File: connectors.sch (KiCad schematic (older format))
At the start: 4 parts

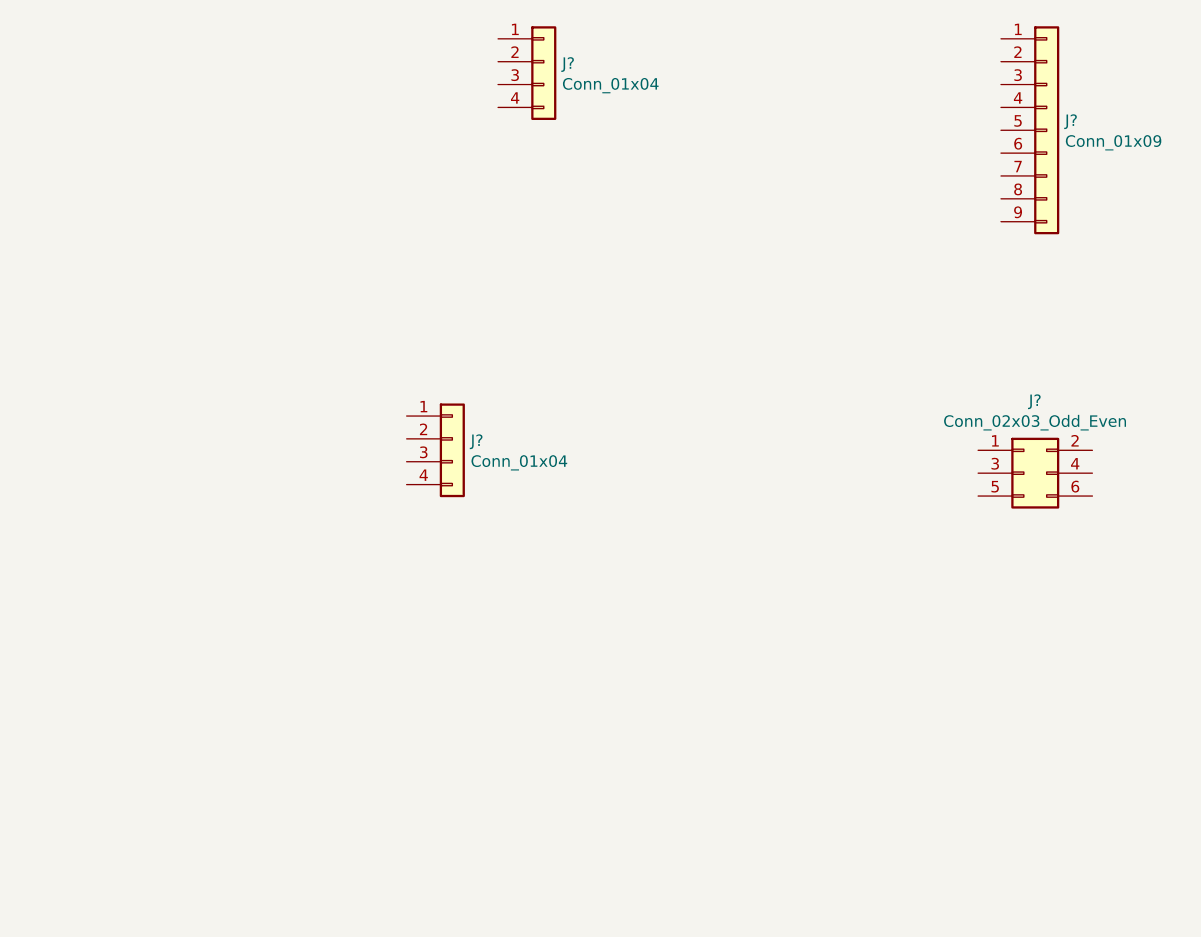
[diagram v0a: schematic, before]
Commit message: Add a new symbol library DS1337_AH to Ahmad library
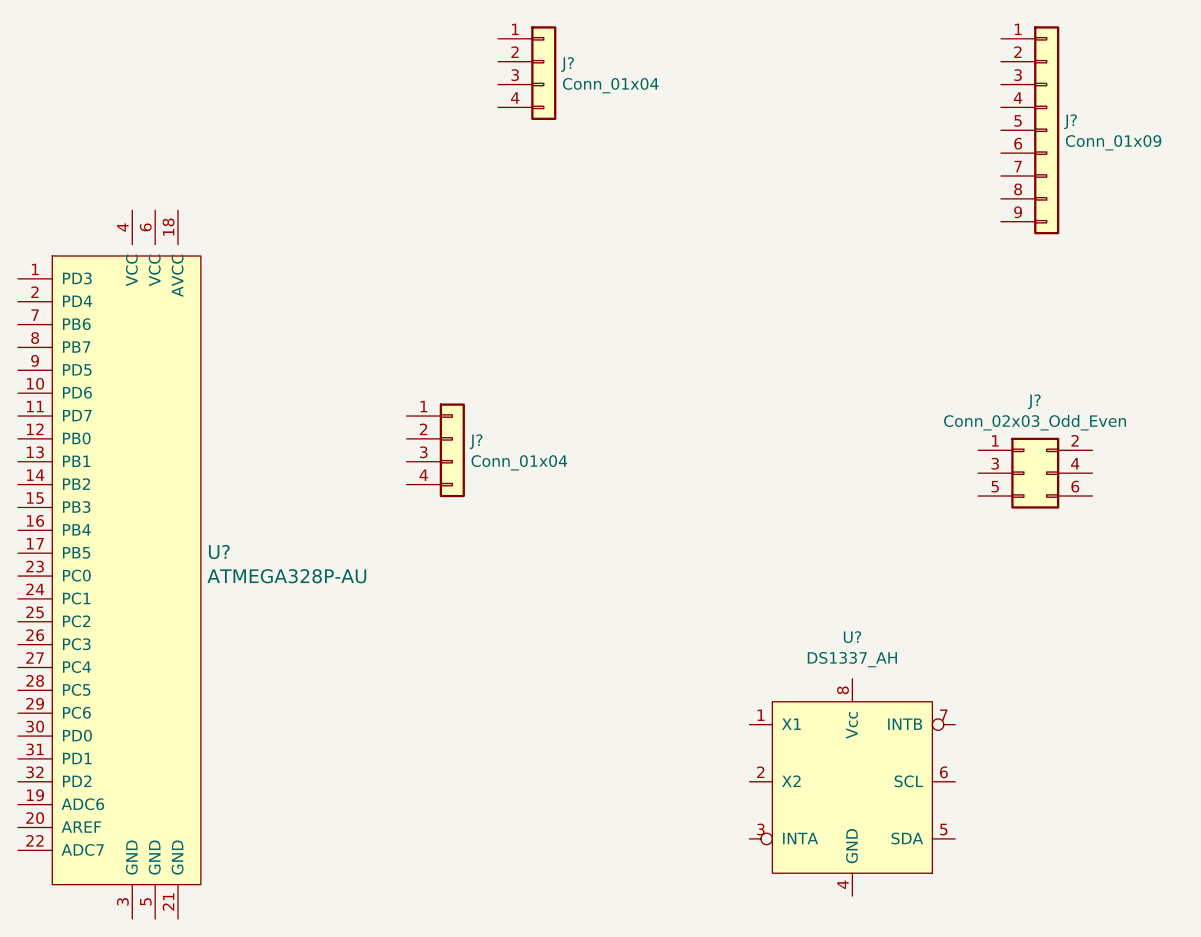
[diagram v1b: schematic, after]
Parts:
- added U?: ATMEGA328P-AU, digikey-footprints:TQFP-32_7x7mm, symbol dk_Embedded-Microcontrollers:ATMEGA328P-AU
- added U?: DS1337_AH, symbol Ahmad_Library:DS1337_AH
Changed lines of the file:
@@
+	1    0    0    -1
+$EndComp
+$Comp
+L dk_Embedded-Microcontrollers:ATMEGA328P-AU U?
+U 1 1 615F99BF
+P 3450 4050
+F 0 "U?" H 3778 4153 60  0000 L CNN
+F 1 "ATMEGA328P-AU" H 3778 4047 60  0000 L CNN
+F 2 "digikey-footprints:TQFP-32_7x7mm" H 3650 4250 60  0001 L CNN
+F 3 "http://www.microchip.com/mymicrochip/filehandler.aspx?ddocname=en608326" H 3650 4350 60  0001 L CNN
+F 4 "ATMEGA328P-AU-ND" H 3650 4450 60  0001 L CNN "Digi-Key_PN"
+F 5 "ATMEGA328P-AU" H 3650 4550 60  0001 L CNN "MPN"
+F 6 "Integrated Circuits (ICs)" H 3650 4650 60  0001 L CNN "Category"
+F 7 "Embedded - Microcontrollers" H 3650 4750 60  0001 L CNN "Family"
+F 8 "http://www.microchip.com/mymicrochip/filehandler.aspx?ddocname=en608326" H 3650 4850 60  0001 L CNN "DK_Datasheet_Link"
+F 9 "/product-detail/en/microchip-technology/ATMEGA328P-AU/ATMEGA328P-AU-ND/1832260" H 3650 4950 60  0001 L CNN "DK_Detail_Page"
+F 10 "IC MCU 8BIT 32KB FLASH 32TQFP" H 3650 5050 60  0001 L CNN "Description"
+F 11 "Microchip Technology" H 3650 5150 60  0001 L CNN "Manufacturer"
+F 12 "Active" H 3650 5250 60  0001 L CNN "Status"
+	1    3450 4050
+	1    0    0    -1
+$EndComp
+$Comp
+L Ahmad_Library:DS1337_AH U?
+U 1 1 615FBA2D
+P 6600 4950
+F 0 "U?" H 6600 5581 50  0000 C CNN
+F 1 "DS1337_AH" H 6600 5490 50  0000 C CNN
+F 2 "" H 6600 5600 50  0001 C CNN
+F 3 "" H 6600 5600 50  0001 C CNN
+	1    6600 4950
 	1    0    0    -1
 $EndComp

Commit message: Complete the association with footprint
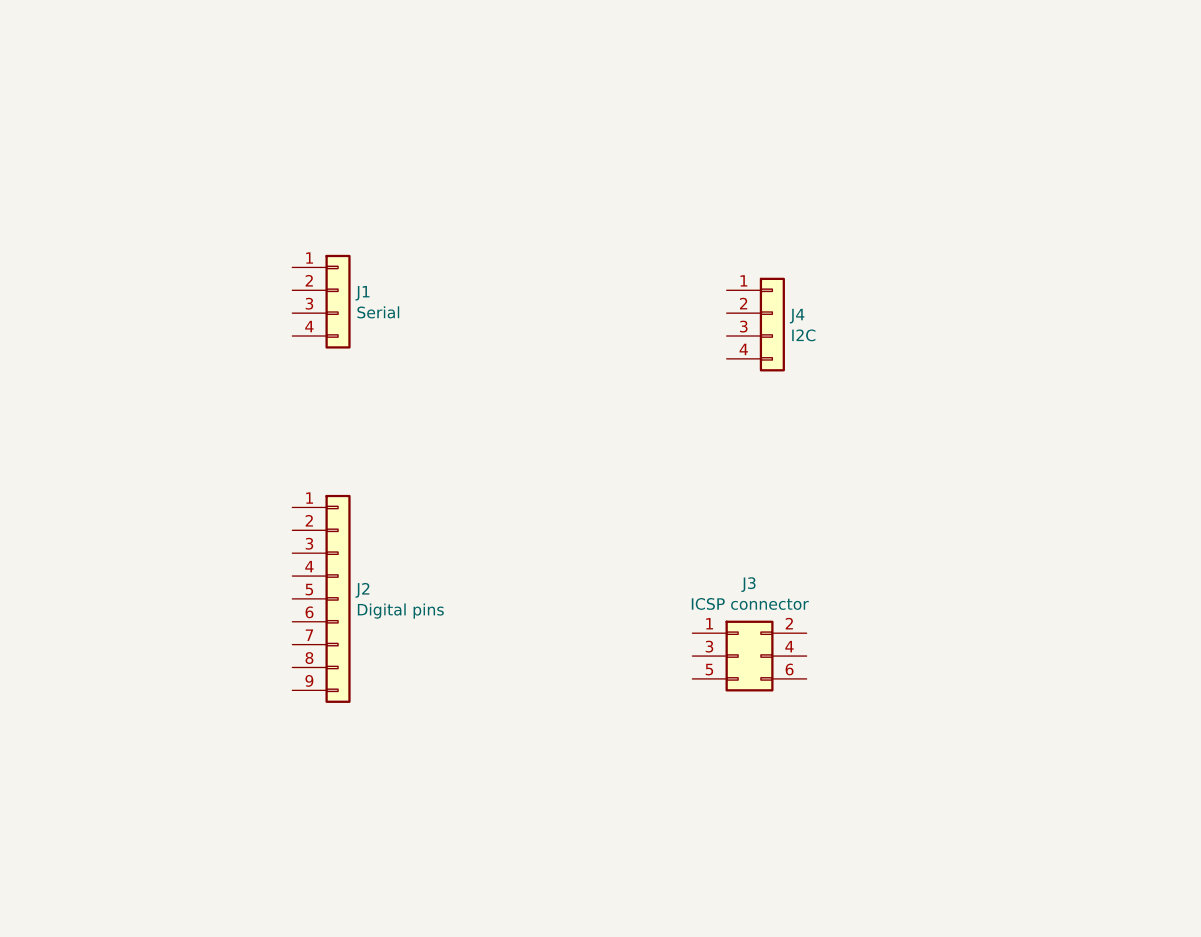
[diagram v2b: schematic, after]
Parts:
- removed U?: ATMEGA328P-AU, digikey-footprints:TQFP-32_7x7mm, symbol dk_Embedded-Microcontrollers:ATMEGA328P-AU
- removed U?: DS1337_AH, symbol Ahmad_Library:DS1337_AH
- J1: renamed from J?; value Conn_01x04 -> Serial; footprint (none) -> Connector_PinSocket_2.54mm:PinSocket_1x04_P2.54mm_Vertical
- J2: renamed from J?; value Conn_01x09 -> Digital pins; footprint (none) -> Connector_PinSocket_2.54mm:PinSocket_1x09_P2.54mm_Vertical
- J3: renamed from J?; value Conn_02x03_Odd_Even -> ICSP connector; footprint (none) -> Connector_PinSocket_2.54mm:PinSocket_2x03_P2.54mm_Vertical
- J4: renamed from J?; value Conn_01x04 -> I2C; footprint (none) -> Connector_PinSocket_2.54mm:PinSocket_1x04_P2.54mm_Vertical
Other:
- moved on the sheet: J1, J2, J3, J4
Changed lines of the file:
@@
 $EndDescr
 $Comp
-L Connector_Generic:Conn_01x09 J?
+L Connector_Generic:Conn_01x09 J2
 U 1 1 615F63B0
-P 7450 2100
-F 0 "J?" H 7530 2142 50  0000 L CNN
-F 1 "Conn_01x09" H 7530 2051 50  0000 L CNN
-F 2 "" H 7450 2100 50  0001 C CNN
-F 3 "~" H 7450 2100 50  0001 C CNN
-	1    7450 2100
+P 4350 4150
+F 0 "J2" H 4430 4192 50  0000 L CNN
+F 1 "Digital pins" H 4430 4101 50  0000 L CNN
+F 2 "Connector_PinSocket_2.54mm:PinSocket_1x09_P2.54mm_Vertical" H 4350 4150 50  0001 C CNN
+F 3 "~" H 4350 4150 50  0001 C CNN
+	1    4350 4150
 	1    0    0    -1
 $EndComp
 $Comp
-L Connector_Generic:Conn_01x04 J?
+L Connector_Generic:Conn_01x04 J1
 U 1 1 615F6E29
-P 5250 1800
-F 0 "J?" H 5330 1792 50  0000 L CNN
-F 1 "Conn_01x04" H 5330 1701 50  0000 L CNN
-F 2 "" H 5250 1800 50  0001 C CNN
-F 3 "~" H 5250 1800 50  0001 C CNN
-	1    5250 1800
+P 4350 2800
+F 0 "J1" H 4430 2792 50  0000 L CNN
+F 1 "Serial" H 4430 2701 50  0000 L CNN
+F 2 "Connector_PinSocket_2.54mm:PinSocket_1x04_P2.54mm_Vertical" H 4350 2800 50  0001 C CNN
+F 3 "~" H 4350 2800 50  0001 C CNN
+	1    4350 2800
 	1    0    0    -1
 $EndComp
 $Comp
-L Connector_Generic:Conn_02x03_Odd_Even J?
+L Connector_Generic:Conn_02x03_Odd_Even J3
 U 1 1 615F7604
-P 7350 3600
-F 0 "J?" H 7400 3917 50  0000 C CNN
-F 1 "Conn_02x03_Odd_Even" H 7400 3826 50  0000 C CNN
-F 2 "" H 7350 3600 50  0001 C CNN
-F 3 "~" H 7350 3600 50  0001 C CNN
-	1    7350 3600
+P 6100 4400
+F 0 "J3" H 6150 4717 50  0000 C CNN
+F 1 "ICSP connector" H 6150 4626 50  0000 C CNN
+F 2 "Connector_PinSocket_2.54mm:PinSocket_2x03_P2.54mm_Vertical" H 6100 4400 50  0001 C CNN
+F 3 "~" H 6100 4400 50  0001 C CNN
+	1    6100 4400
 	1    0    0    -1
 $EndComp
 $Comp
-L Connector_Generic:Conn_01x04 J?
+L Connector_Generic:Conn_01x04 J4
 U 1 1 615F7C9E
-P 4850 3450
-F 0 "J?" H 4930 3442 50  0000 L CNN
-F 1 "Conn_01x04" H 4930 3351 50  0000 L CNN
-F 2 "" H 4850 3450 50  0001 C CNN
-F 3 "~" H 4850 3450 50  0001 C CNN
-	1    4850 3450
+P 6250 2900
+F 0 "J4" H 6330 2892 50  0000 L CNN
+F 1 "I2C" H 6330 2801 50  0000 L CNN
+F 2 "Connector_PinSocket_2.54mm:PinSocket_1x04_P2.54mm_Vertical" H 6250 2900 50  0001 C CNN
+F 3 "~" H 6250 2900 50  0001 C CNN
+	1    6250 2900
 	1    0    0    -1
 $EndComp
-$Comp
-L dk_Embedded-Microcontrollers:ATMEGA328P-AU U?
-U 1 1 615F99BF
-P 3450 4050
-F 0 "U?" H 3778 4153 60  0000 L CNN
-F 1 "ATMEGA328P-AU" H 3778 4047 60  0000 L CNN
-F 2 "digikey-footprints:TQFP-32_7x7mm" H 3650 4250 60  0001 L CNN
-F 3 "http://www.microchip.com/mymicrochip/filehandler.aspx?ddocname=en608326" H 3650 4350 60  0001 L CNN
-F 4 "ATMEGA328P-AU-ND" H 3650 4450 60  0001 L CNN "Digi-Key_PN"
-F 5 "ATMEGA328P-AU" H 3650 4550 60  0001 L CNN "MPN"
-F 6 "Integrated Circuits (ICs)" H 3650 4650 60  0001 L CNN "Category"
-F 7 "Embedded - Microcontrollers" H 3650 4750 60  0001 L CNN "Family"
-F 8 "http://www.microchip.com/mymicrochip/filehandler.aspx?ddocname=en608326" H 3650 4850 60  0001 L CNN "DK_Datasheet_Link"
-F 9 "/product-detail/en/microchip-technology/ATMEGA328P-AU/ATMEGA328P-AU-ND/1832260" H 3650 4950 60  0001 L CNN "DK_Detail_Page"
-F 10 "IC MCU 8BIT 32KB FLASH 32TQFP" H 3650 5050 60  0001 L CNN "Description"
-F 11 "Microchip Technology" H 3650 5150 60  0001 L CNN "Manufacturer"
-F 12 "Active" H 3650 5250 60  0001 L CNN "Status"
-	1    3450 4050
-	1    0    0    -1
-$EndComp
-$Comp
-L Ahmad_Library:DS1337_AH U?
-U 1 1 615FBA2D
-P 6600 4950
-F 0 "U?" H 6600 5581 50  0000 C CNN
-F 1 "DS1337_AH" H 6600 5490 50  0000 C CNN
-F 2 "" H 6600 5600 50  0001 C CNN
-F 3 "" H 6600 5600 50  0001 C CNN
-	1    6600 4950
-	1    0    0    -1
-$EndComp

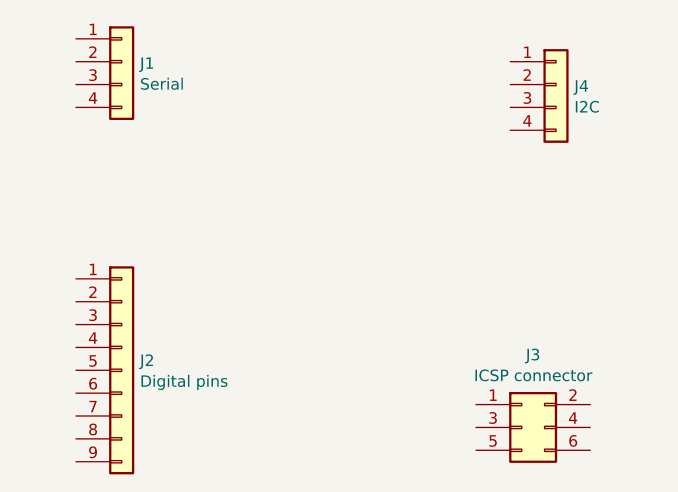
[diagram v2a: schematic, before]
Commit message: Completed the connection in the connectors sheet
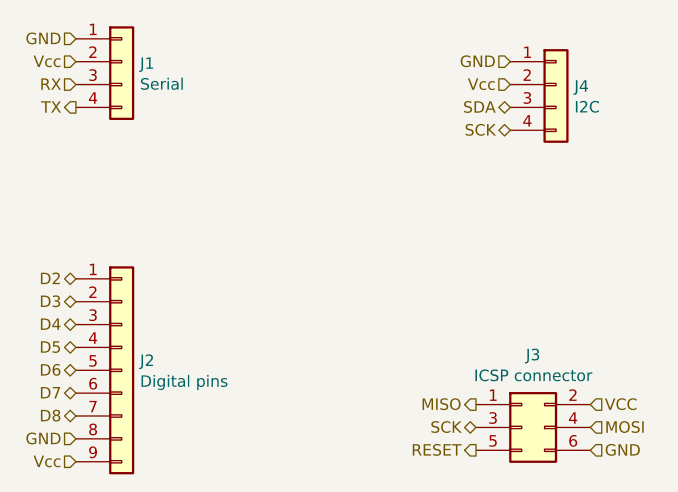
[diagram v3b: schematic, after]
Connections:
- net D2: now reaches J2.1 (Pin_1)
- net D3: now reaches J2.2 (Pin_2)
- net D4: now reaches J2.3 (Pin_3)
- net D5: now reaches J2.4 (Pin_4)
- net D6: now reaches J2.5 (Pin_5)
- net D7: now reaches J2.6 (Pin_6)
- net D8: now reaches J2.7 (Pin_7)
- net GND: now reaches J2.8 (Pin_8)
- net GND: now also J1.1 (Pin_1), J3.6 (Pin_6), J4.1 (Pin_1)
- net Vcc: now reaches J2.9 (Pin_9)
- net Vcc: now also J1.2 (Pin_2), J4.2 (Pin_2)
- net RX: now reaches J1.3 (Pin_3)
- net TX: now reaches J1.4 (Pin_4)
- net MISO: now reaches J3.1 (Pin_1)
- net VCC: now reaches J3.2 (Pin_2)
- net SCK: now reaches J3.3 (Pin_3)
- net SCK: now also J4.4 (Pin_4)
- net MOSI: now reaches J3.4 (Pin_4)
- net RESET: now reaches J3.5 (Pin_5)
- net SDA: now reaches J4.3 (Pin_3)
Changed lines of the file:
@@
 	1    0    0    -1
 $EndComp
+Text HLabel 5900 4300 0    50   Output ~ 0
+MISO
+Text HLabel 5900 4400 0    50   BiDi ~ 0
+SCK
+Text HLabel 5900 4500 0    50   Output ~ 0
+RESET
+Text HLabel 6400 4300 2    50   Input ~ 0
+VCC
+Text HLabel 6400 4400 2    50   Input ~ 0
+MOSI
+Text HLabel 6400 4500 2    50   Input ~ 0
+GND
+Text HLabel 4150 2700 0    50   Input ~ 0
+GND
+Text HLabel 4150 2800 0    50   Input ~ 0
+Vcc
+Text HLabel 4150 2900 0    50   Input ~ 0
+RX
+Text HLabel 4150 3000 0    50   Output ~ 0
+TX
+Text HLabel 6050 2800 0    50   Input ~ 0
+GND
+Text HLabel 6050 2900 0    50   Input ~ 0
+Vcc
+Text HLabel 6050 3000 0    50   BiDi ~ 0
+SDA
+Text HLabel 6050 3100 0    50   BiDi ~ 0
+SCK
+Text HLabel 4150 3750 0    50   BiDi ~ 0
+D2
+Text HLabel 4150 3850 0    50   BiDi ~ 0
+D3
+Text HLabel 4150 3950 0    50   BiDi ~ 0
+D4
+Text HLabel 4150 4050 0    50   BiDi ~ 0
+D5
+Text HLabel 4150 4150 0    50   BiDi ~ 0
+D6
+Text HLabel 4150 4250 0    50   BiDi ~ 0
+D7
+Text HLabel 4150 4350 0    50   BiDi ~ 0
+D8
+Text HLabel 4150 4450 0    50   Input ~ 0
+GND
+Text HLabel 4150 4550 0    50   Input ~ 0
+Vcc
 $EndSCHEMATC

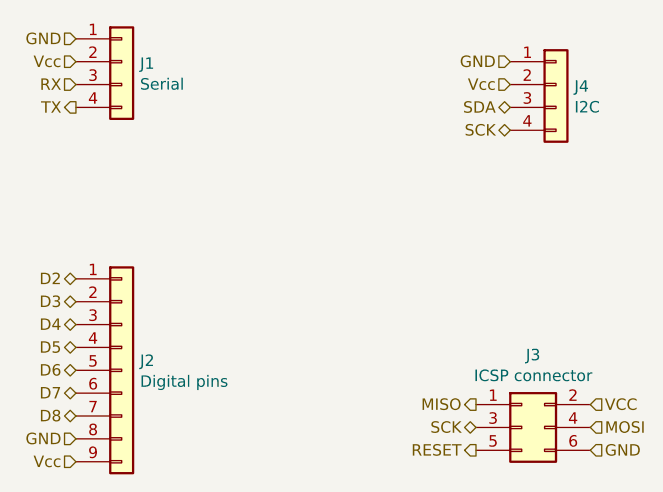
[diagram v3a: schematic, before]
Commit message: Generate a netList
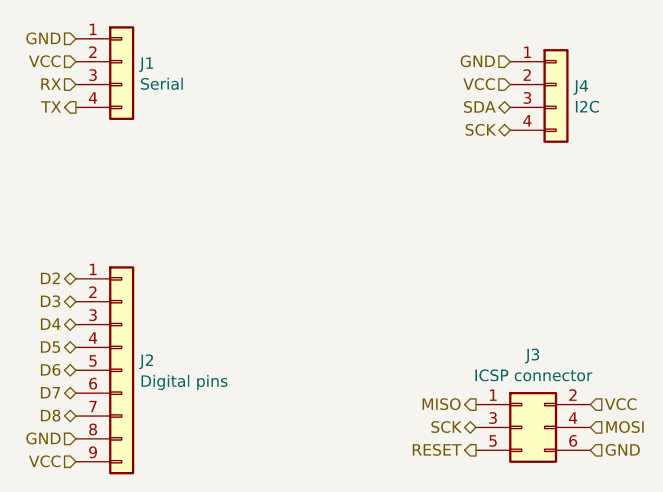
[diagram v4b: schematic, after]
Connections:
- net Vcc is gone; now on net VCC: J1.2 (Pin_2), J2.9 (Pin_9), J4.2 (Pin_2)
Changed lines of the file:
@@
-	1    0    0    -1
-$EndComp
-$Comp
-L Connector_Generic:Conn_01x04 J4
-U 1 1 615F7C9E
-P 6250 2900
-F 0 "J4" H 6330 2892 50  0000 L CNN
-F 1 "I2C" H 6330 2801 50  0000 L CNN
-F 2 "Connector_PinSocket_2.54mm:PinSocket_1x04_P2.54mm_Vertical" H 6250 2900 50  0001 C CNN
-F 3 "~" H 6250 2900 50  0001 C CNN
-	1    6250 2900
 	1    0    0    -1
 $EndComp
@@
 GND
 Text HLabel 4150 2800 0    50   Input ~ 0
-Vcc
+VCC
 Text HLabel 4150 2900 0    50   Input ~ 0
 RX
@@
 GND
 Text HLabel 6050 2900 0    50   Input ~ 0
-Vcc
-Text HLabel 6050 3000 0    50   BiDi ~ 0
-SDA
-Text HLabel 6050 3100 0    50   BiDi ~ 0
-SCK
+VCC
 Text HLabel 4150 3750 0    50   BiDi ~ 0
 D2
@@
 GND
 Text HLabel 4150 4550 0    50   Input ~ 0
-Vcc
+VCC
+Text HLabel 6050 3000 0    50   BiDi ~ 0
+SDA
+$Comp
+L Connector_Generic:Conn_01x04 J4
+U 1 1 615F7C9E
+P 6250 2900
+F 0 "J4" H 6330 2892 50  0000 L CNN
+F 1 "I2C" H 6330 2801 50  0000 L CNN
+F 2 "Connector_PinSocket_2.54mm:PinSocket_1x04_P2.54mm_Vertical" H 6250 2900 50  0001 C CNN
+F 3 "~" H 6250 2900 50  0001 C CNN
+	1    6250 2900
+	1    0    0    -1
+$EndComp
+Text HLabel 6050 3100 0    50   BiDi ~ 0
+SCK
 $EndSCHEMATC
